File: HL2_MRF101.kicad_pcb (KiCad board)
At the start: 4 copper layers, 149.9 x 100 mm, 195 parts, among them CN8 P8, J1 Antenna, J2 HL2, J3 RF3, J4 RF1, J5 RCJ-041, J6 50VDC, J7 12V, J8 Fan, J9 HL2_12V, K1 EC2-3NU, K10 EC2-3NU, K11 EC2-3NU, K12 EC2-3NU, K13 EC2-3NU, K2 EC2-3NU, K3 EC2-3NU, K4 EC2-3NU, K5 EC2-3NU, K6 EC2-3NU, K7 EC2-3NU, K8 EC2-3NU, K9 EC2-3NU, Q1 MRF101AN, Q2 2N7002, Q3 NSS60601MZ4, T1 Coupler, T2 Coupler, T3 744851330, U1 MCP6282E/MS, U3 MCP23008, U4 ULN2003, U5 LM35-NEB, U6 LM393

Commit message: Reworked Op Amps
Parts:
- removed RV2: 10k, Potentiometer_SMD:Potentiometer_Bourns_3314J_Vertical
- removed U6: LM393, Package_SO:SOP-8_3.76x4.96mm_P1.27mm
- added R14: 10k, Resistor_SMD:R_0805_2012Metric, F.Cu at (238.8, 125.3)
- added R38: 12k, Resistor_SMD:R_0805_2012Metric, F.Cu at (246.2, 120.8)
- added TP2: GND, TestPoint:TestPoint_Pad_D1.5mm, F.Cu at (245.8, 124.0)
- added U2: MCP6282E/MS, Package_SO:MSOP-8_3x3mm_P0.65mm, F.Cu at (240.3, 121.6)
- C10, C35: value 180p -> 560p
- C11, C36: value 100p -> 1200p
- C12, C25: value 470p -> 39p
- C13, C26: value 220p -> 56p
- C14, C27: value 150p -> 120p
- C15, C28: value 120p -> 150p
- C16, C29: value 56p -> 220p
- C17, C30: value 39p -> 470p
- C19: value 2200p -> 180p
- C20: value 1200p -> 330p
- C21: value 1000p -> 680p
- C22: value 680p -> 1000p
- C23: value 330p -> 1200p
- C24: value 180p -> 2200p
- C31, C6: value 1200p -> 100p
- C32, C7: value 560p -> 180p
- C33, C8: value 560p -> 390p
- C34, C9: value 390p -> 560p
- L1, L7: value 3.1u -> 224n
- L10, L4: value 680n -> 1.1u
- L11, L5: value 385n -> 1.7u
- L12, L6: value 224n -> 3.1u
- L2, L8: value 1.7u -> 385n
- L3, L9: value 1.1u -> 680n
- R10, R5: value 100k -> 56k
- R34: value 10k -> 62k
- R35: value 560k -> 220k
- R6, R7, R8, R9: footprint Resistor_SMD:R_1206_3216Metric -> Resistor_SMD:R_2512_6332Metric
- TP10: renamed from Band 3
- TP11: renamed from Band 4
- TP12: renamed from Band 5
- TP14: renamed from Band 7
- TP8: renamed from Band 1
- TP9: renamed from Band 2
- moved R6 3.99 mm to (132.9, 64.7), turned to 90 degrees
- moved R9 3.01 mm to (136.9, 50.9), turned to 90 degrees
- moved R8 2.93 mm to (132.9, 50.9), turned to 270 degrees
- moved R7 1.08 mm to (136.9, 64.7), turned to 270 degrees
- moved C18 0.61 mm to (140.1, 63.1)
- moved C37 0.60 mm to (140.1, 52.4)
- moved R11 0.60 mm to (142.5, 52.4)
- moved R4 0.51 mm to (142.6, 63.1)
- renumbered FWD to TP1, RFL to TP3, CN8 to TP6, INTTR to TP7
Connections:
- C79 pad 1: +12V -> +3V3
- R34 pad 1: +12V -> +3V3
- R34 pad 2: Net-(R34-Pad2) -> Net-(C78-Pad1)
- R35 pad 2: Net-(C78-Pad1) -> Net-(R14-Pad2)
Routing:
- net +12V: track 132.9 -> 18.4 mm, vias 2 -> 0
- net Net-(C78-Pad1): track 27.6 -> 0.00 mm, vias 1 -> 0
- net Net-(R34-Pad2): track 9.14 -> 0.00 mm, vias 1 -> 0
- net Net-(R35-Pad1): track 6.60 -> 2.98 mm
- net Net-(R14-Pad1): track 54.8 -> 51.2 mm
- net GND: track 248.6 -> 246.8 mm, vias 197 -> 195
- net Net-(D1-Pad2): track 17.8 -> 19.6 mm
- net Net-(D2-Pad2): track 38.2 -> 39.8 mm

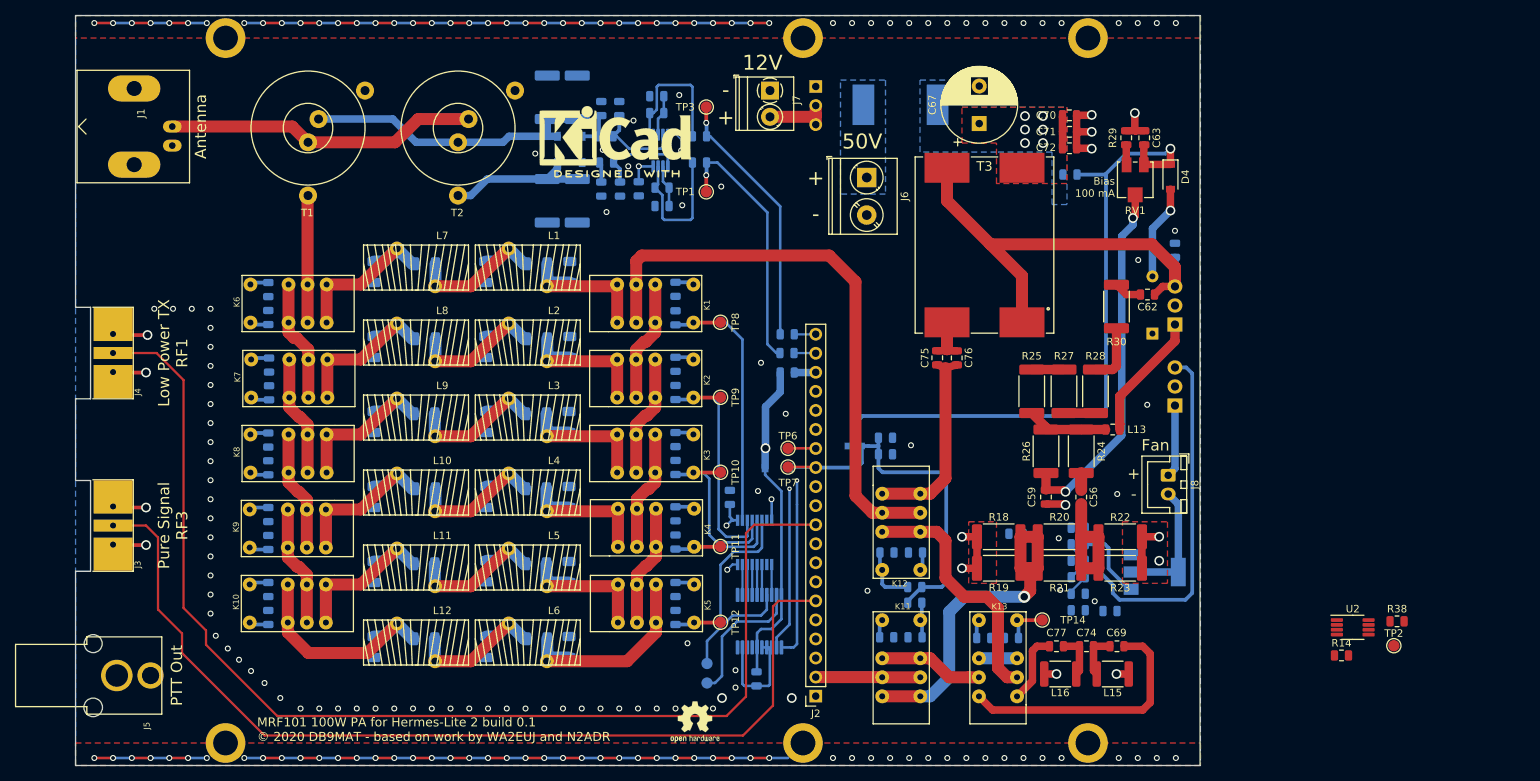
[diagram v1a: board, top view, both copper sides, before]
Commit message: Updated layout
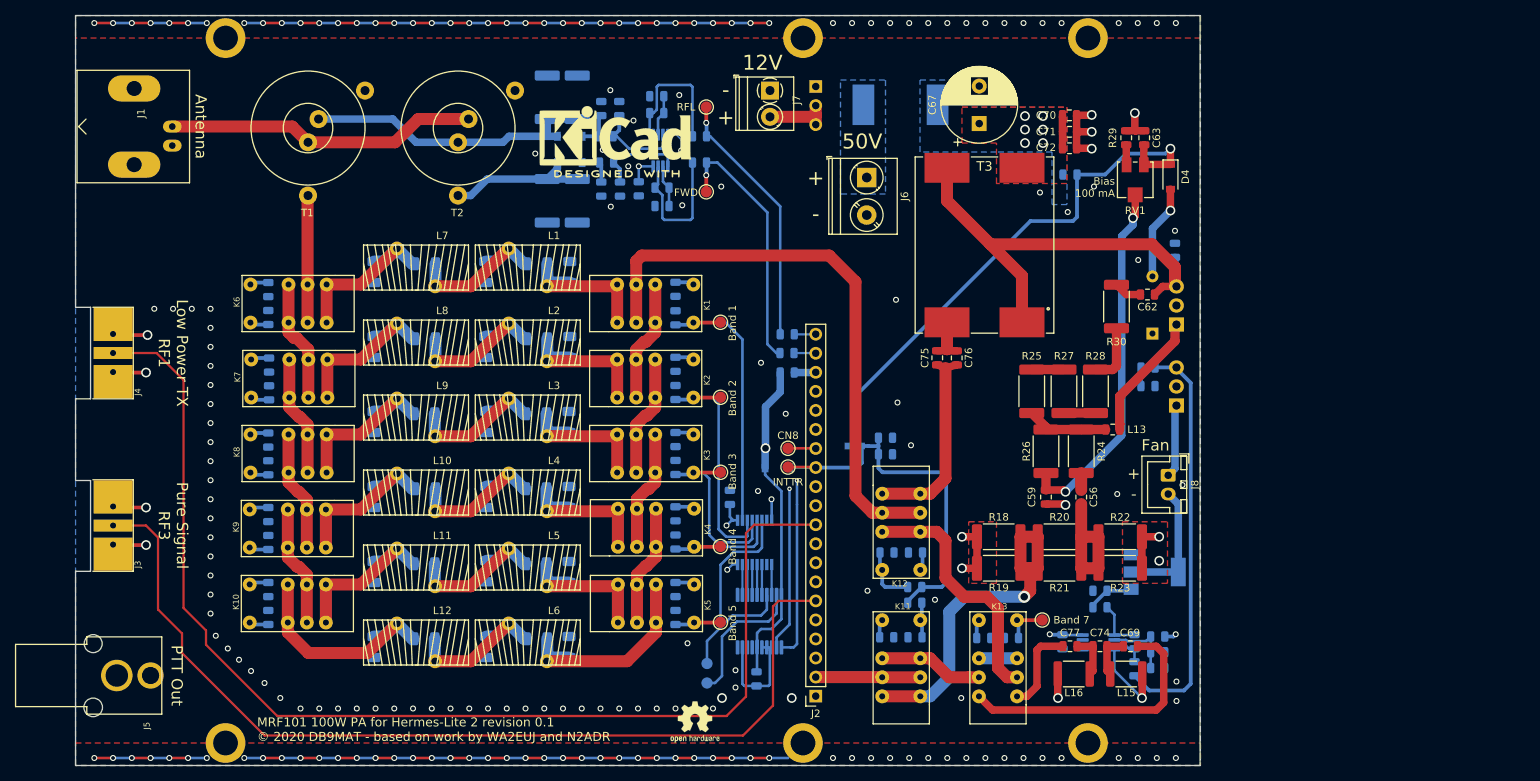
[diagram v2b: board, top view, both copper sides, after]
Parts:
- removed TP2: GND, TestPoint:TestPoint_Pad_D1.5mm
- R14, R38, U2: moved to B.Cu
- moved U2 34.0 mm to (206.4, 123.6), turned to 180 degrees
- moved R38 32.2 mm to (214.3, 124.9)
- moved R33 29.5 mm to (213.0, 86.9), turned to 180 degrees
- moved C61 29.2 mm to (213.0, 89.4)
- moved R14 27.7 mm to (211.2, 127.1), turned to 90 degrees
- moved C79 15.7 mm to (201.6, 123.5), turned to 270 degrees
- moved R35 13.1 mm to (211.2, 123.5), turned to 270 degrees
- moved C78 13.1 mm to (214.3, 127.0)
- moved R36 8.89 mm to (206.6, 118.9), turned to 0 degrees
- moved R37 8.89 mm to (206.6, 116.7)
- moved R34 7.21 mm to (214.3, 122.8), turned to 180 degrees
- moved C69 1.80 mm to (210.7, 124.1)
- moved C74 1.80 mm to (206.6, 124.1)
- moved C77 1.80 mm to (202.6, 124.1)
- moved L15 1.80 mm to (210.1, 127.8)
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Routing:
- net +12V: track 18.4 -> 117.8 mm
- net +3V3: track 358.2 -> 412.8 mm, vias 5 -> 7
- net Net-(C63-Pad2): track 88.8 -> 72.0 mm
- net GND: track 246.8 -> 257.9 mm, vias 195 -> 202
- net Net-(C78-Pad1): track 0.00 -> 9.36 mm
- net Band7: track 49.9 -> 58.3 mm
- net Net-(Q3-Pad1): track 12.4 -> 6.27 mm
- net Net-(R14-Pad2): track 0.03 -> 4.62 mm
- net Net-(R35-Pad1): track 2.98 -> 6.81 mm
- net Net-(R14-Pad1): track 51.2 -> 54.4 mm
- net Net-(C77-Pad1): track 9.44 -> 11.7 mm
- net Net-(C69-Pad2): track 34.4 -> 36.2 mm
- net Net-(C61-Pad1): track 2.98 -> 2.47 mm
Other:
- net class Default: clearance 0.19 -> 0.1
- rule trace_clearance: 0.19 -> 0.1
- board text added: "Band 1"
- board text added: "Band 2"
- board text added: "Band 3"
- board text added: "Band 4"
- board text added: "Band 5"
- board text added: "Band 7"
- board text added: "CN8"
- board text added: "FWD"
- board text added: "INTTR"
- board text added: "JLCJLCJLCJLC"
- board text added: "MRF101 100W PA for Hermes-Lite 2 revision 0.1 © 2020 DB9MAT - based on work by WA2EUJ and N2ADR"
- board text added: "RFL"
- board text removed: "MRF101 100W PA for Hermes-Lite 2 build 0.1 © 2020 DB9MAT - based on work by WA2EUJ and N2ADR"

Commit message: Started current monitor layout
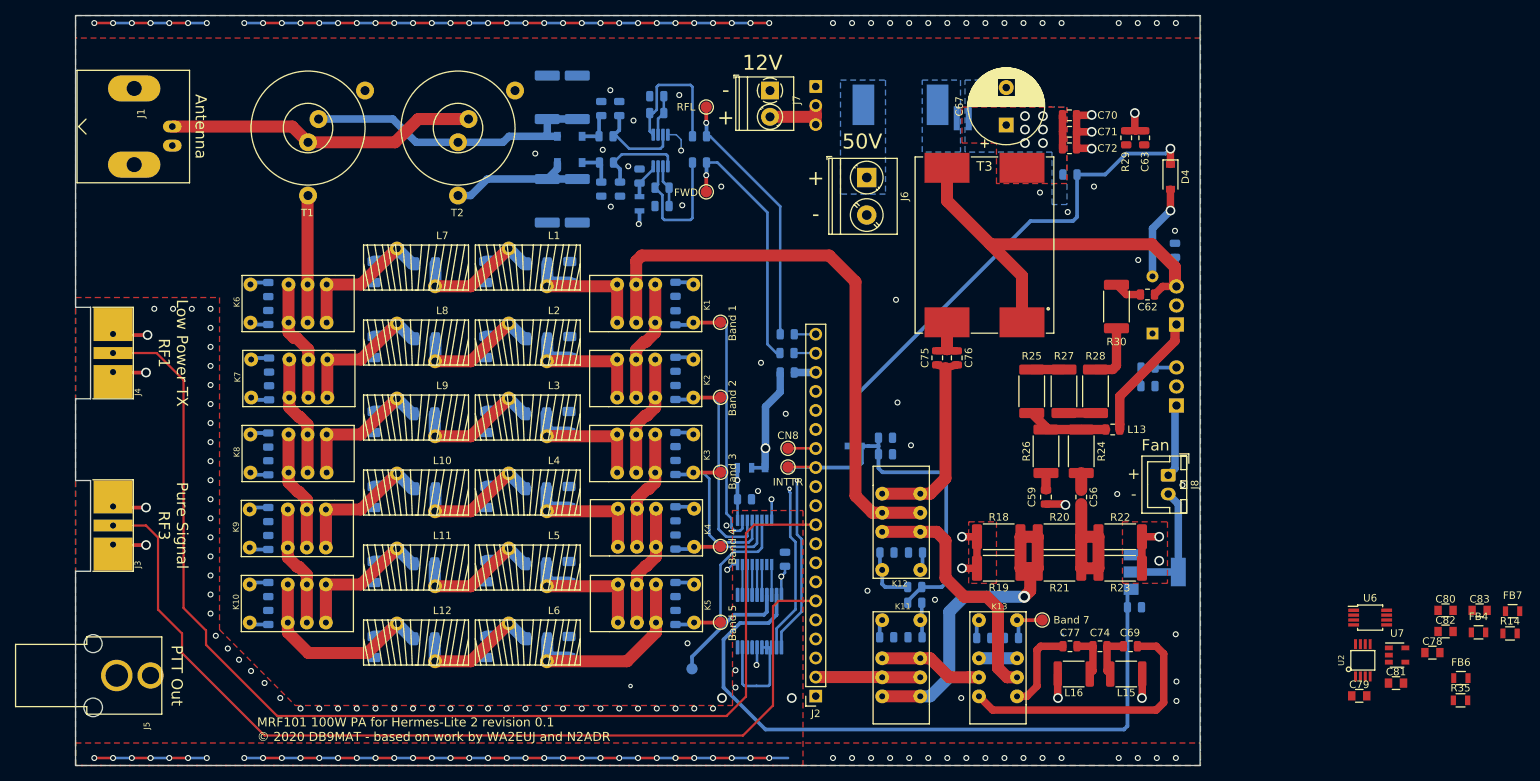
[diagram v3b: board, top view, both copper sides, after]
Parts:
- removed R36: 10k, Resistor_SMD:R_0805_2012Metric
- removed R38: 12k, Resistor_SMD:R_0805_2012Metric
- removed REF**: KiCad-Logo2_8mm_SilkScreen, Symbol:KiCad-Logo2_8mm_SilkScreen
- removed REF** (x2): OSHW-Logo2_7.3x6mm_SilkScreen, Symbol:OSHW-Logo2_7.3x6mm_SilkScreen
- removed REF** (x6): VAL**, n2adr:m3
- removed RV1: 10k, Potentiometer_SMD:Potentiometer_Bourns_3314J_Vertical
- removed TP4: P8, TestPoint:TestPoint_Pad_D1.5mm
- added C80: 4n7, Capacitors_SMD:C_0805, F.Cu at (252.7, 119.3)
- added C81: 100n, Capacitors_SMD:C_0805, F.Cu at (246.1, 129.0)
- added C82: 100n, Capacitors_SMD:C_0805, F.Cu at (252.7, 122.1)
- added C83: DNI, Capacitors_SMD:C_0805, F.Cu at (257.2, 119.3)
- added FB4: FB, Inductors_SMD:L_0805, F.Cu at (257.1, 122.2)
- added FB5: FB, Inductors_SMD:L_0805, B.Cu at (159.2, 100.3)
- added FB6: FB, Inductors_SMD:L_0805, F.Cu at (254.7, 128.3)
- added FB7: FB, Inductors_SMD:L_0805, F.Cu at (261.6, 119.4)
- added FB8: FB, Inductors_SMD:L_0805, B.Cu at (145.2, 65.1)
- added U6: MCP4561, Housings_SSOP:MSOP-8_3x3mm_Pitch0.65mm, F.Cu at (242.6, 120.3)
- added U7: INA193, TO_SOT_Packages_SMD:SOT-23-5, F.Cu at (246.2, 125.3)
- C78: footprint Capacitor_SMD:C_0805_2012Metric -> Capacitors_SMD:C_0805; moved to F.Cu
- C79: value 100n -> 4n7; footprint Capacitor_SMD:C_0805_2012Metric -> Capacitors_SMD:C_0805; moved to F.Cu
- R14: value 10k -> DNI; footprint Resistor_SMD:R_0805_2012Metric -> Resistors_SMD:R_0805; moved to F.Cu
- R34: value 62k -> 0.036; footprint Resistor_SMD:R_0805_2012Metric -> Resistors_SMD:R_0612
- R35: value 220k -> DNI; footprint Resistor_SMD:R_0805_2012Metric -> Resistors_SMD:R_0805; moved to F.Cu
- U2: value MCP6282E/MS -> MAX11613; footprint Package_SO:MSOP-8_3x3mm_P0.65mm -> n2adr:MAX11613; moved to F.Cu
- moved R34 73.8 mm to (188.3, 53.7)
- moved R14 50.3 mm to (261.3, 122.4), turned to 0 degrees
- moved R35 44.2 mm to (254.7, 131.3), turned to 0 degrees
- moved C79 40.2 mm to (241.2, 130.7), turned to 0 degrees
- moved C78 36.7 mm to (250.9, 125.0)
- moved U2 35.3 mm to (241.7, 126.0), turned to 0 degrees
- moved C54 16.4 mm to (164.6, 112.5), turned to 270 degrees
- moved R37 5.10 mm to (211.2, 118.9), turned to 180 degrees
- moved C67 3.61 mm to (194.1, 54.6)
- moved TP5 2.12 mm to (152.2, 127.1)
- moved C55 1.97 mm to (159.2, 104.5), turned to 180 degrees
- moved C47 1.70 mm to (145.2, 61.4), turned to 270 degrees
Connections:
- C47 pad 2: +3V3 -> Net-(C47-Pad2)
- C54 pad 2: +3V3 -> Net-(C54-Pad2)
- C55 pad 2: +3V3 -> Net-(C54-Pad2)
- C78 pad 1: Net-(C78-Pad1) -> GND
- C78 pad 2: GND -> Net-(C78-Pad2)
- C79 pad 1: +3V3 -> GND
- C79 pad 2: GND -> Vipa
- L14 pad 2: Net-(C67-Pad1) -> Net-(L14-Pad2)
- Q3 pad 1: Net-(Q3-Pad1) -> Fan_Ctrl
- R14 pad 1: Net-(R14-Pad1) -> Net-(C83-Pad1)
- R14 pad 2: Net-(R14-Pad2) -> Net-(L14-Pad2)
- R32 pad 1: Net-(C67-Pad1) -> Net-(L14-Pad2)
- R33 pad 1: Net-(R14-Pad1) -> Vtemp
- R34 pad 1: +3V3 -> Net-(C67-Pad1)
- R34 pad 2: Net-(C78-Pad1) -> Net-(L14-Pad2)
- R35 pad 1: Net-(R35-Pad1) -> Net-(C83-Pad2)
- R35 pad 2: Net-(R14-Pad2) -> Net-(C67-Pad1)
- R37 pad 2: Net-(Q3-Pad1) -> Fan_Ctrl
- U1 pad 8: +3V3 -> Net-(C47-Pad2)
- U2 pad 1: Net-(R35-Pad1) -> Vtemp
- U2 pad 2: Net-(C78-Pad1) -> Vipa
- U2 pad 3: Net-(R14-Pad2) -> Net-(U2-Pad3)
- U2 pad 4: GND -> Net-(U2-Pad4)
- U2 pad 5: (no net) -> SCL
- U2 pad 6: (no net) -> SDA
- U2 pad 7: (no net) -> GND
- U2 pad 8: +3V3 -> Net-(C78-Pad2)
- U3 pad 19: Net-(TP4-Pad1) -> Fan_Ctrl
- U3 pad 20: +3V3 -> Net-(C54-Pad2)
- U4 pad 9: +3V3 -> Net-(C54-Pad2)
- U5 pad 3: Net-(R14-Pad1) -> Vtemp
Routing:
- net Fan_Ctrl: track 0.00 -> 92.3 mm
- net Net-(R14-Pad1): track 54.4 -> 0.00 mm
- net Net-(C59-Pad1): track 48.4 -> 2.26 mm, vias 2 -> 0
- net +3V3: track 412.8 -> 371.7 mm
- net Net-(C54-Pad2): track 0.00 -> 26.3 mm, vias 0 -> 2
- net Net-(TP4-Pad1): track 18.7 -> 0.00 mm
- net Net-(C78-Pad1): track 9.36 -> 0.00 mm
- net GND: track 257.9 -> 249.9 mm, vias 202 -> 203
- net Net-(R35-Pad1): track 6.81 -> 0.00 mm
- net Net-(Q3-Pad1): track 6.27 -> 0.00 mm
- net Net-(C63-Pad2): track 72.0 -> 65.8 mm
- net Net-(C47-Pad2): track 0.00 -> 4.79 mm
- net Net-(R14-Pad2): track 4.62 -> 0.00 mm
- net Band1: track 102.2 -> 105.2 mm
- net Vtemp: track 0.00 -> 2.86 mm
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- added copper zone on B.Cu, net Net-(L14-Pad2)
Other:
- board text removed: "Bias 100 mA"

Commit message: Further routing
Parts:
- added MH: VAL**, n2adr:m3, F.Cu at (90.0, 43.0)
- added MH: VAL**, n2adr:m3, F.Cu at (167.0, 43.0)
- added MH: VAL**, n2adr:m3, F.Cu at (206.0, 43.0)
- added MH: VAL**, n2adr:m3, F.Cu at (205.0, 137.0)
- added MH: VAL**, n2adr:m3, F.Cu at (168.0, 137.0)
- added MH: VAL**, n2adr:m3, F.Cu at (90.0, 137.0)
- added REF**: OSHW-Symbol_6.7x6mm_SilkScreen, Symbol:OSHW-Symbol_6.7x6mm_SilkScreen, B.Cu at (153.7, 135.2)
- added REF**: OSHW-Symbol_6.7x6mm_SilkScreen, Symbol:OSHW-Symbol_6.7x6mm_SilkScreen, F.Cu at (153.7, 135.2)
- added REF**: KiCad-Logo2_8mm_SilkScreen, Symbol:KiCad-Logo2_8mm_SilkScreen, F.Cu at (141.9, 56.4)
- added REF**: ESD-Logo_8.9x8mm_SilkScreen, Symbol:ESD-Logo_8.9x8mm_SilkScreen, F.Cu at (79.5, 69.9)
- C78, C79, C80, C81, C82, C83: footprint Capacitors_SMD:C_0805 -> Capacitor_SMD:C_0805_2012Metric; moved to B.Cu
- FB4, FB6, FB7: footprint Inductors_SMD:L_0805 -> Inductor_SMD:L_0805_2012Metric; moved to B.Cu
- FB5, FB8: footprint Inductors_SMD:L_0805 -> Inductor_SMD:L_0805_2012Metric
- R14, R35: value DNI -> JNC; footprint Resistors_SMD:R_0805 -> Resistor_SMD:R_0805_2012Metric; moved to B.Cu
- R34: footprint Resistors_SMD:R_0612 -> Resistor_SMD:R_0612_1632Metric
- U2: moved to B.Cu
- U6: footprint Housings_SSOP:MSOP-8_3x3mm_Pitch0.65mm -> Package_SO:MSOP-8_3x3mm_P0.65mm; moved to B.Cu
- U7: footprint TO_SOT_Packages_SMD:SOT-23-5 -> Package_TO_SOT_SMD:SOT-23-5; moved to B.Cu
- moved R14 97.7 mm to (187.2, 58.6), turned to 90 degrees
- moved R35 97.6 mm to (189.5, 58.6), turned to 90 degrees
- moved C83 90.1 mm to (188.3, 61.3)
- moved FB6 88.4 mm to (192.6, 65.4)
- moved C79 85.6 mm to (183.3, 67.7)
- moved C80 85.2 mm to (183.3, 69.9)
- moved U7 84.0 mm to (188.3, 64.5)
- moved FB4 82.9 mm to (192.6, 70.1), turned to 180 degrees
- moved C81 81.4 mm to (192.6, 67.7)
- moved C78 78.5 mm to (192.6, 72.4), turned to 180 degrees
- moved U2 76.3 mm to (187.5, 72.2)
- moved FB7 74.9 mm to (200.0, 76.8)
- moved C82 68.0 mm to (200.0, 79.1)
- moved U6 65.8 mm to (194.1, 75.8)
- moved C76 0.30 mm to (187.2, 85.7)
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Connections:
- R32 pad 1: Net-(L14-Pad2) -> Net-(C67-Pad1)
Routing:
- net +3V3: track 371.7 -> 497.3 mm, vias 7 -> 10
- net Vtemp: track 2.86 -> 48.0 mm, vias 0 -> 2
- net SDA: track 35.3 -> 79.7 mm, vias 1 -> 3
- net Net-(C59-Pad1): track 2.26 -> 41.9 mm, vias 0 -> 1
- net SCL: track 36.5 -> 75.2 mm
- net Net-(C63-Pad2): track 65.8 -> 97.9 mm, vias 1 -> 4
- net Net-(R29-Pad1): track 0.00 -> 32.1 mm, vias 0 -> 3
- net GND: track 249.9 -> 261.7 mm, vias 203 -> 205
- net Net-(C78-Pad2): track 0.00 -> 8.80 mm
- net Vipa: track 0.00 -> 7.64 mm
- net Net-(C82-Pad1): track 0.00 -> 5.16 mm
- net Net-(C81-Pad1): track 0.00 -> 4.57 mm
- net Net-(C83-Pad2): track 0.00 -> 4.02 mm
- net Net-(C83-Pad1): track 0.00 -> 3.98 mm
- net Net-(J2-Pad10): track 156.0 -> 157.2 mm
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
